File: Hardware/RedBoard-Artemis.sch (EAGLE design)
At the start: 84 parts, among them IC3 LM1117, J2 CORTEX_DEBUG, J3 POWER_JACKTOE, J5 USB-C, Q1 1.1A/60V/600mΩ, U1 ARTEMIS_MODULESMD, U3 AP2112-3.3V, U5 CH340C, Y1 32.768kHz

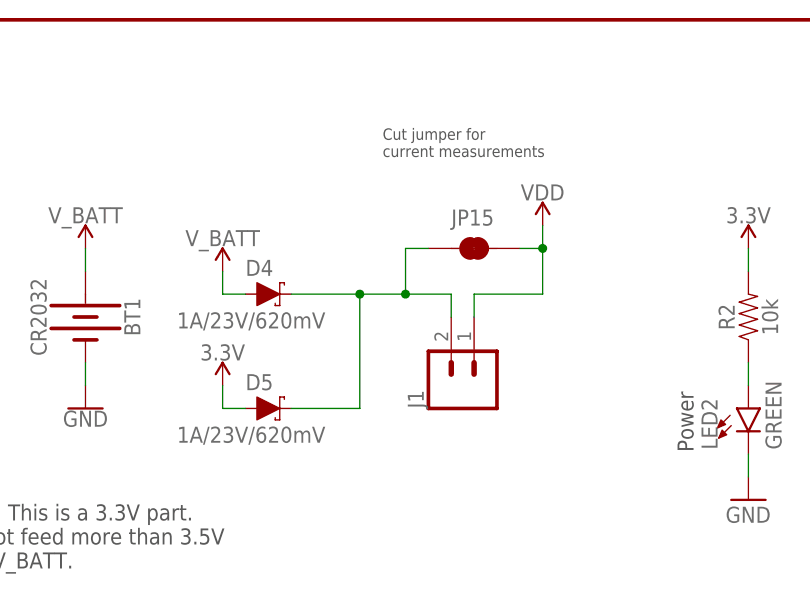
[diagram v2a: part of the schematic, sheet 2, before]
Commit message: Remove diode from 3.3V rail. Move MEAS jumper.
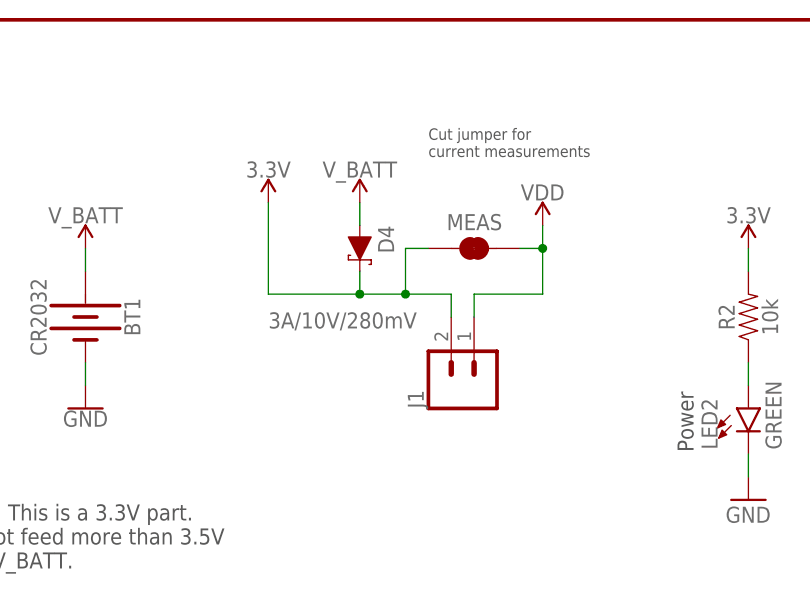
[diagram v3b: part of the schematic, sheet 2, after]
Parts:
- removed D5: 1A/23V/620mV, SparkFun-DiscreteSemi:DIODE-SCHOTTKY-BAT20J
- D4: value 1A/23V/620mV -> 3A/10V/280mV; device SparkFun-DiscreteSemi:DIODE-SCHOTTKY-BAT20J -> SparkFun-DiscreteSemi:DIODE-SCHOTTKY-BAT60A
- renumbered JP15 to MEAS
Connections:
- removed net N$3: D4.C, D5.C, J1.2, MEAS.1
- net 3.3V: now also D4.C, J1.2, MEAS.1; no longer D5.A
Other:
- moved on the sheet: D4
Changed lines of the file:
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@@
 <?xml version="1.0" encoding="utf-8"?>
 <!DOCTYPE eagle SYSTEM "eagle.dtd">
-<eagle version="9.4.0">
+<eagle version="9.4.2">
 <drawing>
 <settings>
@@
 <part name="GND30" library="SparkFun-PowerSymbols" deviceset="GND" device=""/>
 <part name="U$7" library="SparkFun-PowerSymbols" deviceset="5V" device=""/>
-<part name="D4" library="SparkFun-DiscreteSemi" deviceset="DIODE-SCHOTTKY" device="-BAT20J" value="1A/23V/620mV"/>
-<part name="D5" library="SparkFun-DiscreteSemi" deviceset="DIODE-SCHOTTKY" device="-BAT20J" value="1A/23V/620mV"/>
+<part name="D4" library="SparkFun-DiscreteSemi" deviceset="DIODE-SCHOTTKY" device="-BAT60A" value="3A/10V/280mV"/>
 <part name="SUPPLY10" library="SparkFun-PowerSymbols" deviceset="V_BATT" device=""/>
 <part name="SUPPLY11" library="SparkFun-PowerSymbols" deviceset="VDD" device=""/>
@@
 <part name="SUPPLY1" library="SparkFun-PowerSymbols" deviceset="3.3V" device=""/>
 <part name="J1" library="SparkFun-Connectors" deviceset="CONN_02" device="1X02_NO_SILK"/>
-<part name="JP15" library="SparkFun-Jumpers" deviceset="JUMPER-SMT_2_NC_TRACE" device="_SILK" value=""/>
+<part name="MEAS" library="SparkFun-Jumpers" deviceset="JUMPER-SMT_2_NC_TRACE" device="_SILK" value=""/>
 <part name="Y1" library="SparkFun-Clocks" deviceset="CRYSTAL-32.768KHZ" device="SMD-3.2X1.5" value="32.768kHz"/>
 <part name="C11" library="SparkFun-Capacitors" deviceset="15PF" device="-0603-50V-5%" value="15pF"/>
@@
 <text x="106.68" y="134.62" size="1.778" layer="97" font="vector">3.3V
 600mA Out</text>
-<text x="187.96" y="170.18" size="1.27" layer="97">Cut jumper for
+<text x="193.04" y="170.18" size="1.27" layer="97">Cut jumper for
 current measurements</text>
 <text x="122.174" y="180.086" size="2.54" layer="94" font="vector" ratio="15" align="center">Power Supplies</text>
@@
 <attribute name="VALUE" x="101.6" y="162.814" size="1.778" layer="96" align="bottom-center"/>
 </instance>
-<instance part="D4" gate="G$1" x="175.26" y="154.94" smashed="yes">
-<attribute name="NAME" x="172.72" y="156.972" size="1.778" layer="95" font="vector"/>
-<attribute name="VALUE" x="165.1" y="152.908" size="1.778" layer="96" font="vector" align="top-left"/>
-</instance>
-<instance part="D5" gate="G$1" x="175.26" y="142.24" smashed="yes">
-<attribute name="NAME" x="172.72" y="144.272" size="1.778" layer="95" font="vector"/>
-<attribute name="VALUE" x="165.1" y="140.208" size="1.778" layer="96" font="vector" align="top-left"/>
-</instance>
-<instance part="SUPPLY10" gate="G$1" x="170.18" y="157.48" smashed="yes">
-<attribute name="VALUE" x="170.18" y="160.274" size="1.778" layer="96" align="bottom-center"/>
+<instance part="D4" gate="G$1" x="185.42" y="160.02" smashed="yes" rot="R270">
+<attribute name="NAME" x="187.452" y="162.56" size="1.778" layer="95" font="vector" rot="R270"/>
+<attribute name="VALUE" x="175.26" y="152.908" size="1.778" layer="96" font="vector" align="top-left"/>
+</instance>
+<instance part="SUPPLY10" gate="G$1" x="185.42" y="165.1" smashed="yes">
+<attribute name="VALUE" x="185.42" y="167.894" size="1.778" layer="96" align="bottom-center"/>
 </instance>
 <instance part="SUPPLY11" gate="VDD" x="205.74" y="162.56" smashed="yes">
@@
 <attribute name="VALUE" x="154.94" y="141.986" size="1.778" layer="96" align="top-center"/>
 </instance>
-<instance part="SUPPLY17" gate="G$1" x="170.18" y="144.78" smashed="yes">
-<attribute name="VALUE" x="170.18" y="147.574" size="1.778" layer="96" align="bottom-center"/>
+<instance part="SUPPLY17" gate="G$1" x="175.26" y="165.1" smashed="yes">
+<attribute name="VALUE" x="175.26" y="167.894" size="1.778" layer="96" align="bottom-center"/>
 </instance>
 <instance part="SUPPLY1" gate="G$1" x="137.16" y="160.02" smashed="yes">
@@
 <attribute name="NAME" x="192.532" y="142.24" size="1.778" layer="95" font="vector" rot="R90"/>
 </instance>
-<instance part="JP15" gate="G$1" x="198.12" y="160.02" smashed="yes">
-<attribute name="NAME" x="195.58" y="162.56" size="1.778" layer="95" font="vector"/>
+<instance part="MEAS" gate="G$1" x="198.12" y="160.02" smashed="yes">
+<attribute name="NAME" x="195.072" y="162.052" size="1.778" layer="95" font="vector"/>
 <attribute name="VALUE" x="195.58" y="157.48" size="1.778" layer="96" font="vector" align="top-left"/>
 </instance>
@@
 <net name="3.3V" class="0">
 <segment>
-<pinref part="D5" gate="G$1" pin="A"/>
-<wire x1="172.72" y1="142.24" x2="170.18" y2="142.24" width="0.1524" layer="91"/>
-<wire x1="170.18" y1="142.24" x2="170.18" y2="144.78" width="0.1524" layer="91"/>
+<wire x1="175.26" y1="154.94" x2="175.26" y2="165.1" width="0.1524" layer="91"/>
 <pinref part="SUPPLY17" gate="G$1" pin="3.3V"/>
+<pinref part="D4" gate="G$1" pin="C"/>
+<wire x1="185.42" y1="154.94" x2="185.42" y2="157.48" width="0.1524" layer="91"/>
+<wire x1="185.42" y1="154.94" x2="190.5" y2="154.94" width="0.1524" layer="91"/>
+<junction x="185.42" y="154.94"/>
+<pinref part="J1" gate="G$1" pin="2"/>
+<wire x1="190.5" y1="154.94" x2="195.58" y2="154.94" width="0.1524" layer="91"/>
+<wire x1="195.58" y1="154.94" x2="195.58" y2="152.4" width="0.1524" layer="91"/>
+<pinref part="MEAS" gate="G$1" pin="1"/>
+<wire x1="193.04" y1="160.02" x2="190.5" y2="160.02" width="0.1524" layer="91"/>
+<wire x1="190.5" y1="160.02" x2="190.5" y2="154.94" width="0.1524" layer="91"/>
+<junction x="190.5" y="154.94"/>
+<wire x1="175.26" y1="154.94" x2="185.42" y2="154.94" width="0.1524" layer="91"/>
 </segment>
 <segment>
@@
 <wire x1="198.12" y1="154.94" x2="205.74" y2="154.94" width="0.1524" layer="91"/>
 <wire x1="205.74" y1="154.94" x2="205.74" y2="160.02" width="0.1524" layer="91"/>
-<pinref part="JP15" gate="G$1" pin="2"/>
+<pinref part="MEAS" gate="G$1" pin="2"/>
 <wire x1="205.74" y1="160.02" x2="203.2" y2="160.02" width="0.1524" layer="91"/>
 <pinref part="SUPPLY11" gate="VDD" pin="VDD"/>
@@
 <segment>
 <pinref part="D4" gate="G$1" pin="A"/>
-<wire x1="172.72" y1="154.94" x2="170.18" y2="154.94" width="0.1524" layer="91"/>
+<wire x1="185.42" y1="162.56" x2="185.42" y2="165.1" width="0.1524" layer="91"/>
 <pinref part="SUPPLY10" gate="G$1" pin="V_BATT"/>
-<wire x1="170.18" y1="154.94" x2="170.18" y2="157.48" width="0.1524" layer="91"/>
 </segment>
 <segment>
@@
 </segment>
 </net>
-<net name="N$3" class="0">
-<segment>
-<pinref part="D5" gate="G$1" pin="C"/>
-<wire x1="177.8" y1="142.24" x2="185.42" y2="142.24" width="0.1524" layer="91"/>
-<wire x1="185.42" y1="142.24" x2="185.42" y2="154.94" width="0.1524" layer="91"/>
-<pinref part="D4" gate="G$1" pin="C"/>
-<wire x1="185.42" y1="154.94" x2="177.8" y2="154.94" width="0.1524" layer="91"/>
-<wire x1="185.42" y1="154.94" x2="190.5" y2="154.94" width="0.1524" layer="91"/>
-<junction x="185.42" y="154.94"/>
-<pinref part="J1" gate="G$1" pin="2"/>
-<wire x1="190.5" y1="154.94" x2="195.58" y2="154.94" width="0.1524" layer="91"/>
-<wire x1="195.58" y1="154.94" x2="195.58" y2="152.4" width="0.1524" layer="91"/>
-<pinref part="JP15" gate="G$1" pin="1"/>
-<wire x1="193.04" y1="160.02" x2="190.5" y2="160.02" width="0.1524" layer="91"/>
-<wire x1="190.5" y1="160.02" x2="190.5" y2="154.94" width="0.1524" layer="91"/>
-<junction x="190.5" y="154.94"/>
-</segment>
-</net>

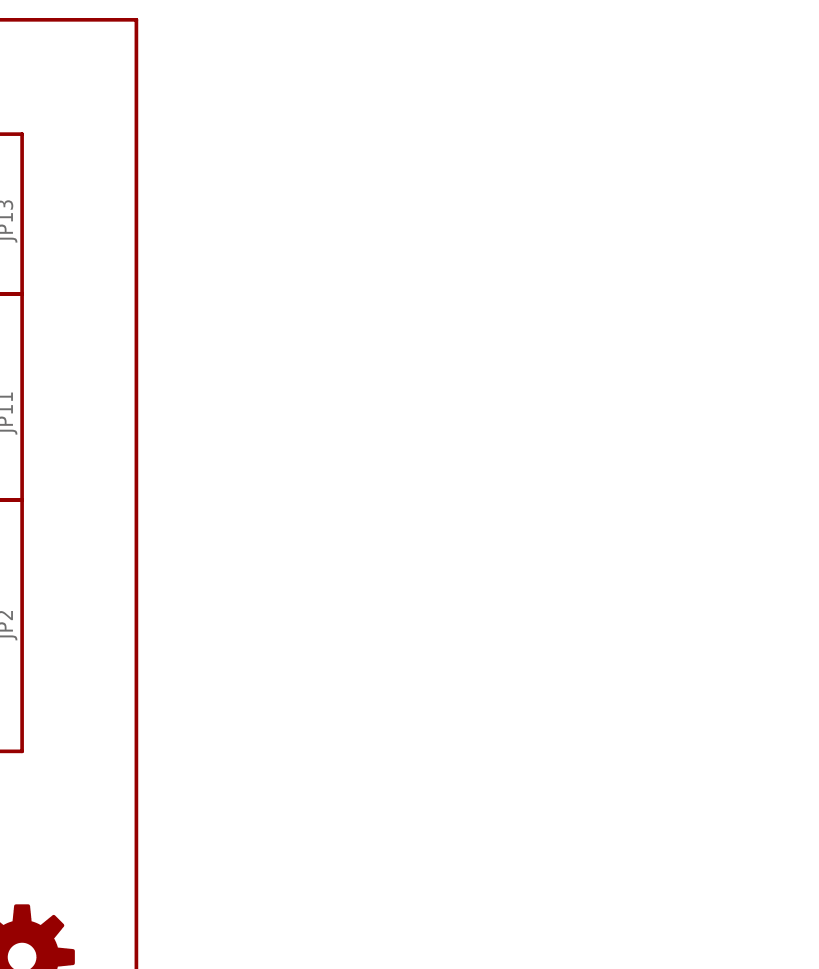
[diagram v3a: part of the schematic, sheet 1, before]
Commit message: Add PTH connectors to edges of board.
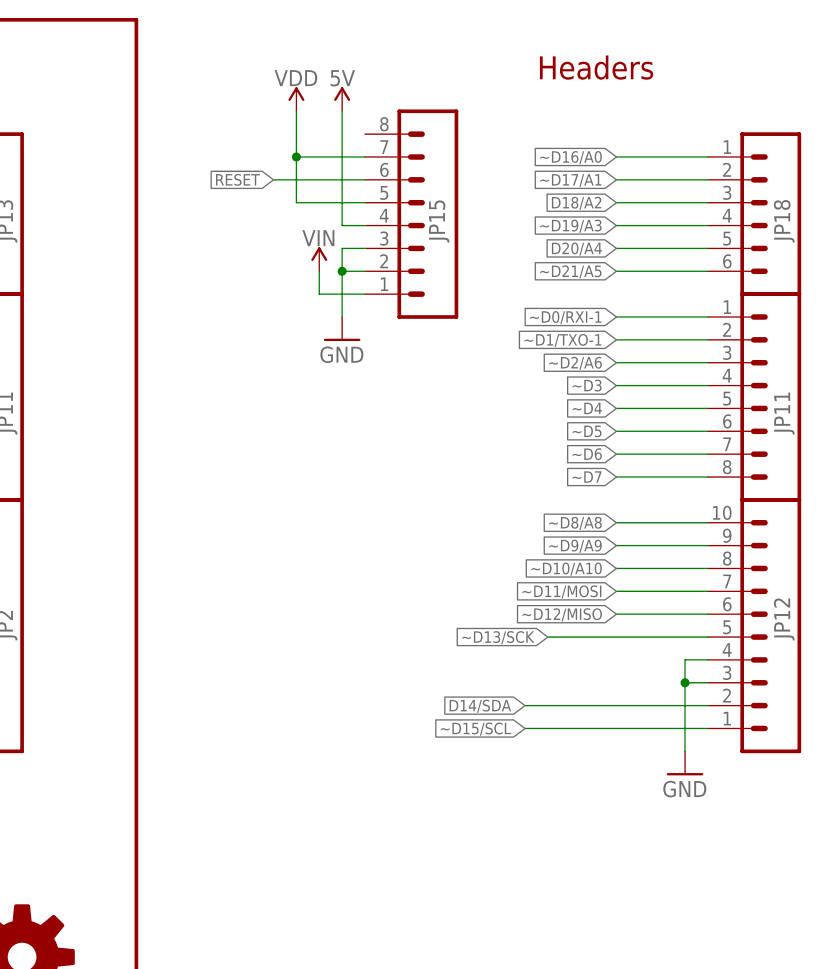
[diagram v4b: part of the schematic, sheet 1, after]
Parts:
- added JP12: M10NO_SILK, SparkFun-Connectors:M10NO_SILK
- added JP15: (no value), SparkFun-Connectors:M08NO_SILK
- added JP17: JP11, SparkFun-Connectors:M08NO_SILK
- added JP18: (no value), SparkFun-Connectors:M06NO_SILK
- Q1: value 1.1A/60V/600mΩ -> 2.5A/30V/105mΩ; device SparkFun-DiscreteSemi:MOSFET_PCH-SI2309DS -> SparkFun-DiscreteSemi:MOSFET_PCH-DMG2307L
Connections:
- net !RESET: now also JP15.6
- net 5V: now also JP15.4
- net D14/SDA: now also JP12.2
- net D18/A2: now also JP18.3
- net D20/A4: now also JP18.5
- net GND: now also JP12.3, JP12.4, JP15.2, JP15.3
- net VDD: now also JP15.5, JP15.7
- net VIN: now also JP15.1
- net ~D0/RXI-1: now also JP17.1
- net ~D1/TXO-1: now also JP17.2
- net ~D10/A10: now also JP12.8
- net ~D11/MOSI: now also JP12.7
- net ~D12/MISO: now also JP12.6
- net ~D13/SCK: now also JP12.5
- net ~D15/SCL: now also JP12.1
- net ~D16/A0: now also JP18.1
- net ~D17/A1: now also JP18.2
- net ~D19/A3: now also JP18.4
- net ~D2/A6: now also JP17.3
- net ~D21/A5: now also JP18.6
- net ~D3: now also JP17.4
- net ~D4: now also JP17.5
- net ~D5: now also JP17.6
- net ~D6: now also JP17.7
- net ~D7: now also JP17.8
- net ~D8/A8: now also JP12.10
- net ~D9/A9: now also JP12.9

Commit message: Add bottom silk indicators. Move MEAS jumper.
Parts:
- removed FRAME1: FRAME-LETTER, SparkFun-Aesthetics:FRAME-LETTER
- removed FRAME2: FRAME-LETTERNO_PACKAGE, SparkFun-Aesthetics:FRAME-LETTERNO_PACKAGE
- removed MEAS: JUMPER-SMT_2_NC_TRACE_SILK, SparkFun-Jumpers:JUMPER-SMT_2_NC_TRACE_SILK
- added FRAME3: FRAME-LEDGER, SparkFun-Aesthetics:FRAME-LEDGER
- added JP19: (no value), SparkFun-Connectors:CONN_08NO_SILK_FEMALE_PTH
- JP10, JP11: device SparkFun-Connectors:M08SMD-COMBO -> SparkFun-Connectors:CONN_08SMD-COMBO-FEMALE_NC
- JP17: value JP11 -> MEAS; device SparkFun-Connectors:M08NO_SILK -> SparkFun-Jumpers:JUMPER-SMT_2_NC_TRACE_SILK; PROD_ID CONN-10204 -> (none)
- U1: device Testing:ARTEMIS_MODULESMD -> SparkFun-IC-Microcontroller:ARTEMIS_MODULESMD
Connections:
- net 3.3V: now also JP17.1; no longer MEAS.1
- net VDD: now also JP17.2; no longer MEAS.2
- net ~D0/RXI-1: now also JP19.1; no longer JP17.1
- net ~D1/TXO-1: now also JP19.2; no longer JP17.2
- net ~D2/A6: now also JP19.3; no longer JP17.3
- net ~D3: now also JP19.4; no longer JP17.4
- net ~D4: now also JP19.5; no longer JP17.5
- net ~D5: now also JP19.6; no longer JP17.6
- net ~D6: now also JP19.7; no longer JP17.7
- net ~D7: now also JP19.8; no longer JP17.8
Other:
- note added: "Optional IO Masters broken out to SMD pads"
- note added: "PTH Headers"
- note added: "SMD Headers"
- note removed: "Headers"
- note removed: "Optional Bus Masters broken out to SMD pads"
